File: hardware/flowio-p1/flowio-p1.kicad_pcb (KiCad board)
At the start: 4 copper layers, 90 x 75 mm, 139 parts, among them J1 DC-005, J10 VALVE, J11 VALVE, J12 VALVE, J13 VALVE, J14 VALVE, J15 VALVE, J16 VALVE, J17 VALVE, J18 DEBUG-UART, J19 DEBUG-GPIO, J2 USB-C, J5 XH-4P, J6 XH-4P, J7 XH-4P, J8 XH-4P, J9 XH-4P, Q10 AO3400A, Q11 SS8050, Q12 SS8050, Q3 AO3400A, Q4 AO3400A, Q5 AO3400A, Q6 AO3400A, Q7 AO3400A, Q8 AO3400A, Q9 AO3400A, SW1 RST, SW2 BOOT, SW3 USER, U1 ESP32-S3-WROOM-1-N16R8, U2 TCA9548APWR, U3 TPS54331DR, U4 CH340K, U5 USBLC6-2SC6

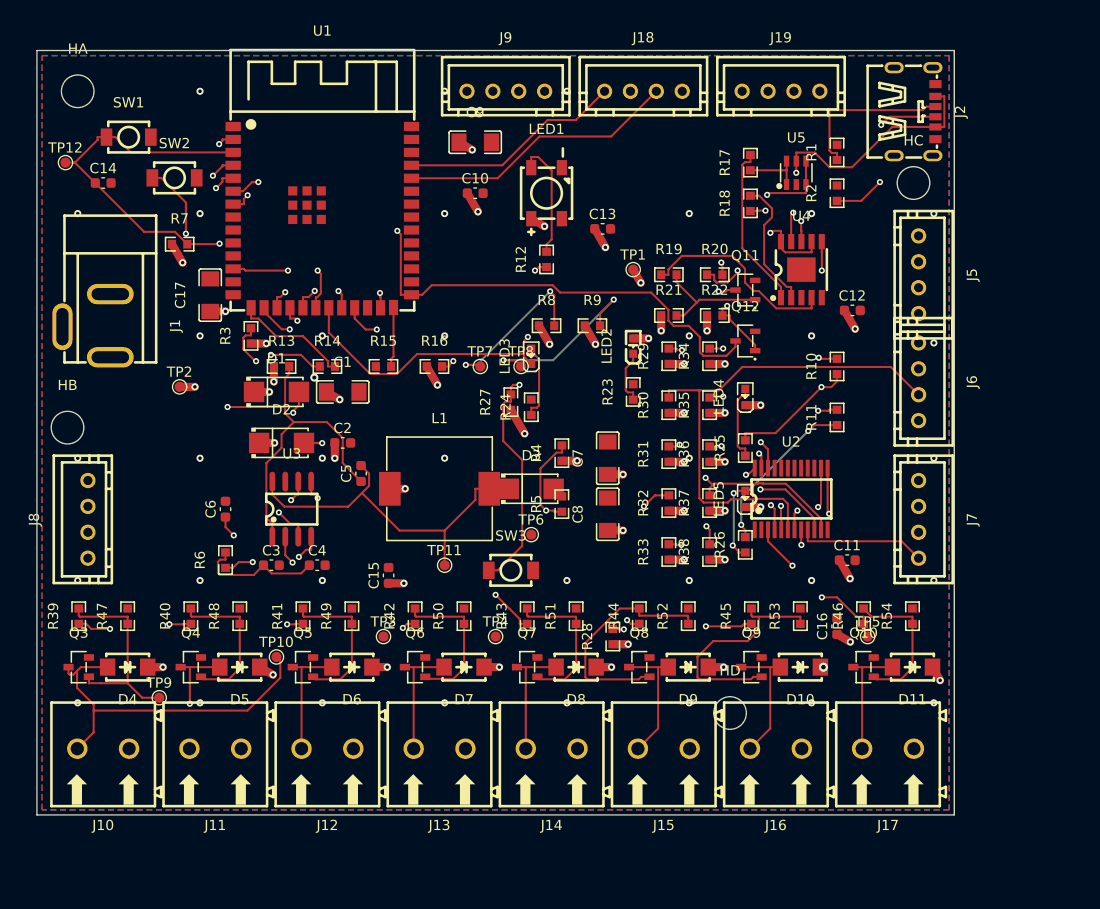
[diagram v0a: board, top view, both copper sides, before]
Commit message: feat(pcb): DRC 攻坚 17→6 未连接·其余 error 类全零 (freerouting 三轮+自研 boardgeom/netdoctor 全障碍路由)
- boardgeom: 点对旋转矩形精确距离/分层走线校验/过孔孔距规则/禁布区+板边建模
- netdoctor: 填充岛探测(PIP)/岛间跳线/焊盘逃逸/In1-In2-B.Cu 多层 BFS 路由
- 修复: 天线禁布区找回·HD移位·D10/C16/C15/C3/U3.2 电源锚·U2/U5 GND 逃逸
  (U5.2 via-in-pad)·J2.CC 走线绕行·TP8 微移·R13/R14/R29 strap 供电·GND 碎片缝合
- 遗留 6 未连接需 GUI 收尾: R13 簇/R29 簇/C3-U3.2 簇×2/GND zone 对/3V3 zone 对
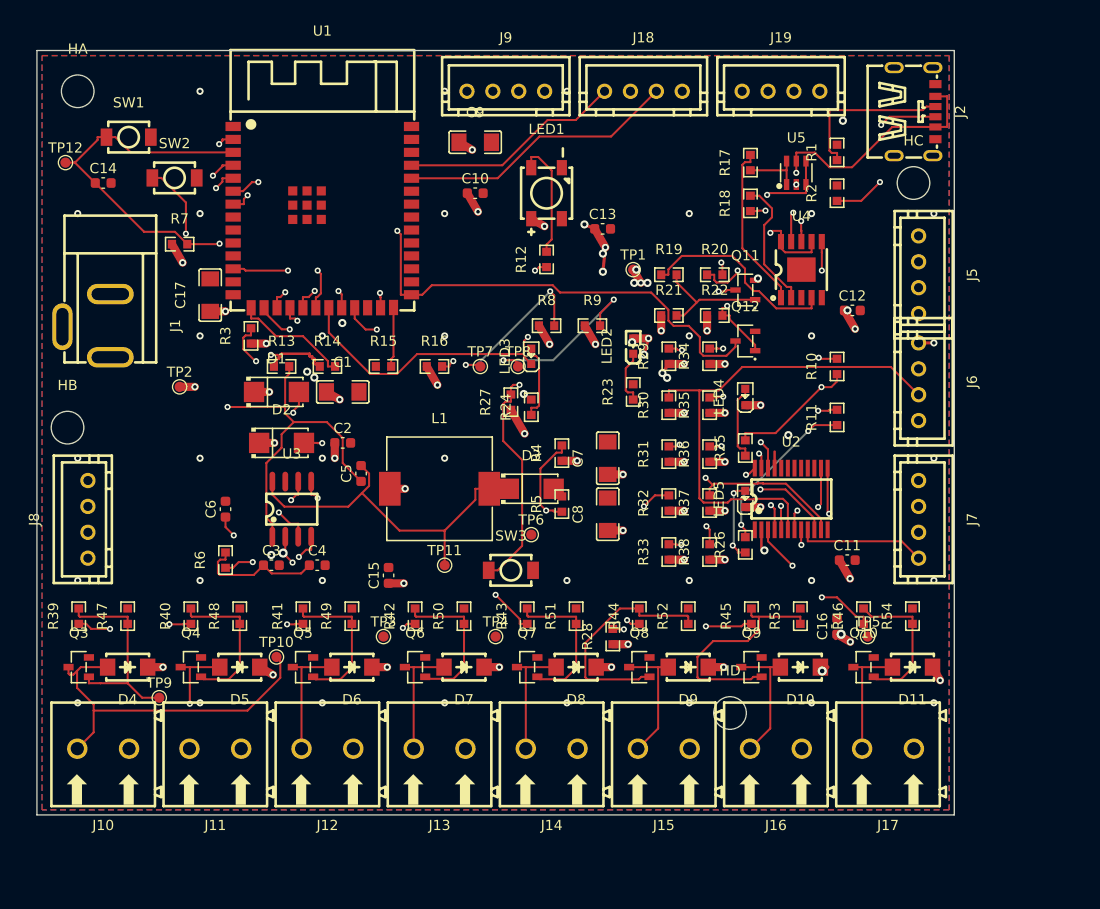
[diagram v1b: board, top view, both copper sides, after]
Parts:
- moved TP8 0.30 mm to (47.2, 31.0)
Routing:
- net +5V: track 32.8 -> 55.2 mm, vias 18 -> 20
- net +3V3: track 122.2 -> 130.5 mm, vias 39 -> 48
- net GND: track 0.00 -> 3.65 mm, vias 35 -> 44
- net USB_VBUS: track 86.6 -> 87.1 mm

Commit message: feat(pcb): T1 KRT repair_planes 全层修复 → 未连接 6→0, error 类全零!
- GND F/B/In1 + 3V3(12区11路)/5V(6区5路) In2 平面断区全接
- oracle_reconnect 连带解决 R13/R14/C3-U3.2 口袋簇 (6→0 超预期)
- 剩余仅外观类: silk_over_copper 54 + courtyard 44+13 (豁免清单)
- 环境补装 scipy/shapely + rust grid_router v0.22 + kicad_oracle v10 上游bug补丁
- 附注: min_hole_clearance 25→20 (JLC 经济档合规) + 8处 via-in-pad 需 IPC-4761 Type VII
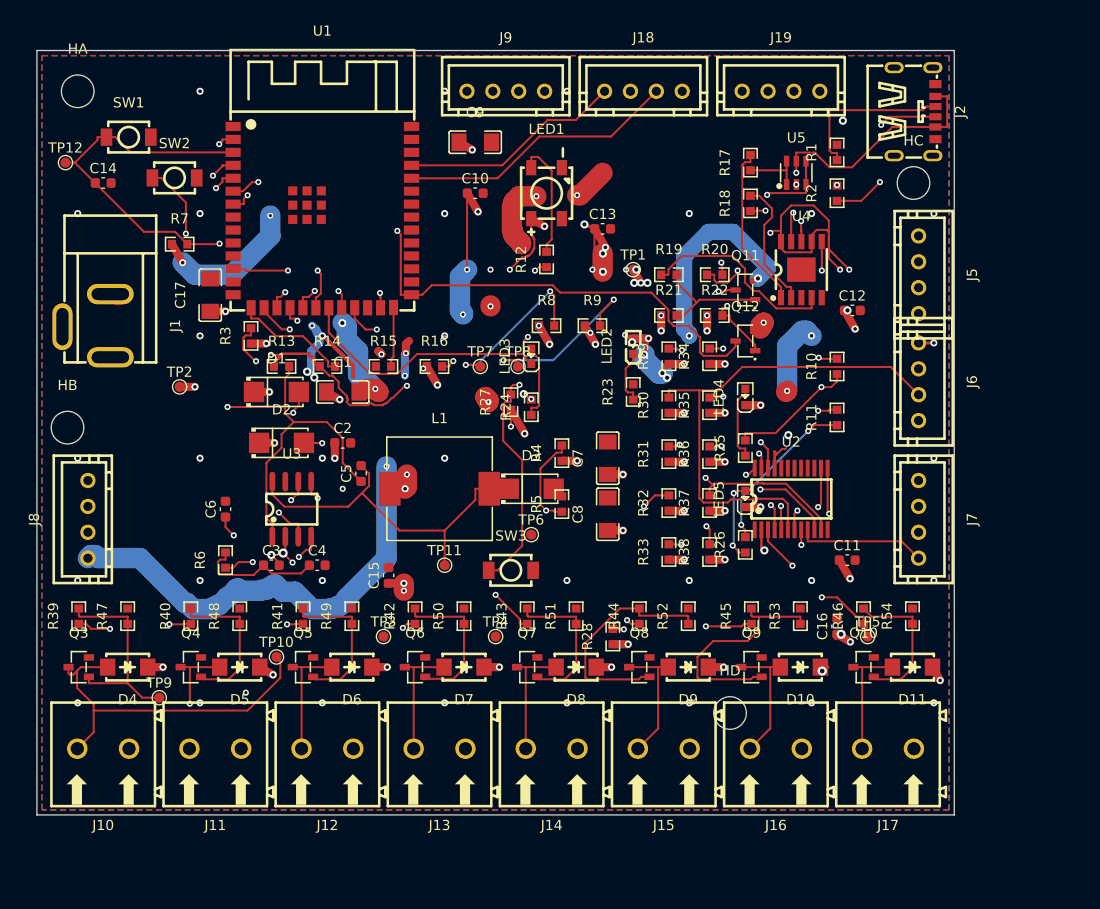
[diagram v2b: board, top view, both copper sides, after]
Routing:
- net +3V3: track 130.5 -> 285.5 mm, vias 48 -> 66
- net GND: track 3.65 -> 138.8 mm, vias 44 -> 60
- net +5V: track 55.2 -> 84.6 mm, vias 20 -> 21

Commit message: feat(T3b): PCB 重布局 100x80 + 五缺陷修复 + 26 新件 — DRC error 归零
布局 (spec T3):
- 板框 90x75 -> 100x80: 底边 J10-J17 阀带 (11mm 节距) + 右边 J20-J23 主阀/泵带
  + 传感带重排 (J5 底右角/J6 左壁/J7 顶右角, 为右边缘主阀带让位)
- 新增 PLACE: J20-J23 + R55-64/Q13-16/D12-15 右侧驱动列 (与 Q3-Q10 同域) +
  U6 XGZP6897D (44,22, LOCAL 内联手建封装: 排距7.96/节距2.54/焊盘0.9x2.0) +
  C18 + U7/R63/R64 (J1 USB-C CC 防护) + TP13 (DRV_PUMP)
- 安装孔: HA(3.4,3.4)/HC(83,12)/HB(3,28)/HD(73.5,55.7) — HD 避 J15/J16+D9 双冲突

五缺陷修复 (spec §1):
1. C9 移 (63,55) 出 J9 XH 壳体投影 (原 43,9)
2. R3 移 (21,34) 出 U1 WROOM 禁布 (本体下缘 26.1 + 3mm)
3. HD 移位 + case_geom.ST 同步 (见 T3c) — 钻孔对拍由 L2 测试守门
4. route_pcb.py: npth_min 2.0->3.5 (过孔-铜柱环外缘净空, 板界 100x80,
   缝合栅格扩展) — T4 布线不再复发; MANUAL 干线表标废弃待 T4 重推导
5. 端子高度 offset: WJ500V->XH-2P 换型自然消解 (h 14.07->6.2)

连带清除 P1.0 遗留 courtyard 冲突 (44 项): Q-D 列距 ±2.4->±3.0/+2.5,
上拉梯/LED 列/下载三极管/buck 输出链重排, SW1/SW2/R1/R2/R10/R11 微调
设计规则: 板边铜净空 0.5->0.3 (显式, JLC ≥0.3)
产物: flowio-p1.kicad_pcb (164 封装) + drc.rpt (0 error) + fab/ 全套重出
(pos 147 refs / drl M3=T5@新孔位 / gerber / BOM 39 行 146 refs / pos-jlc)
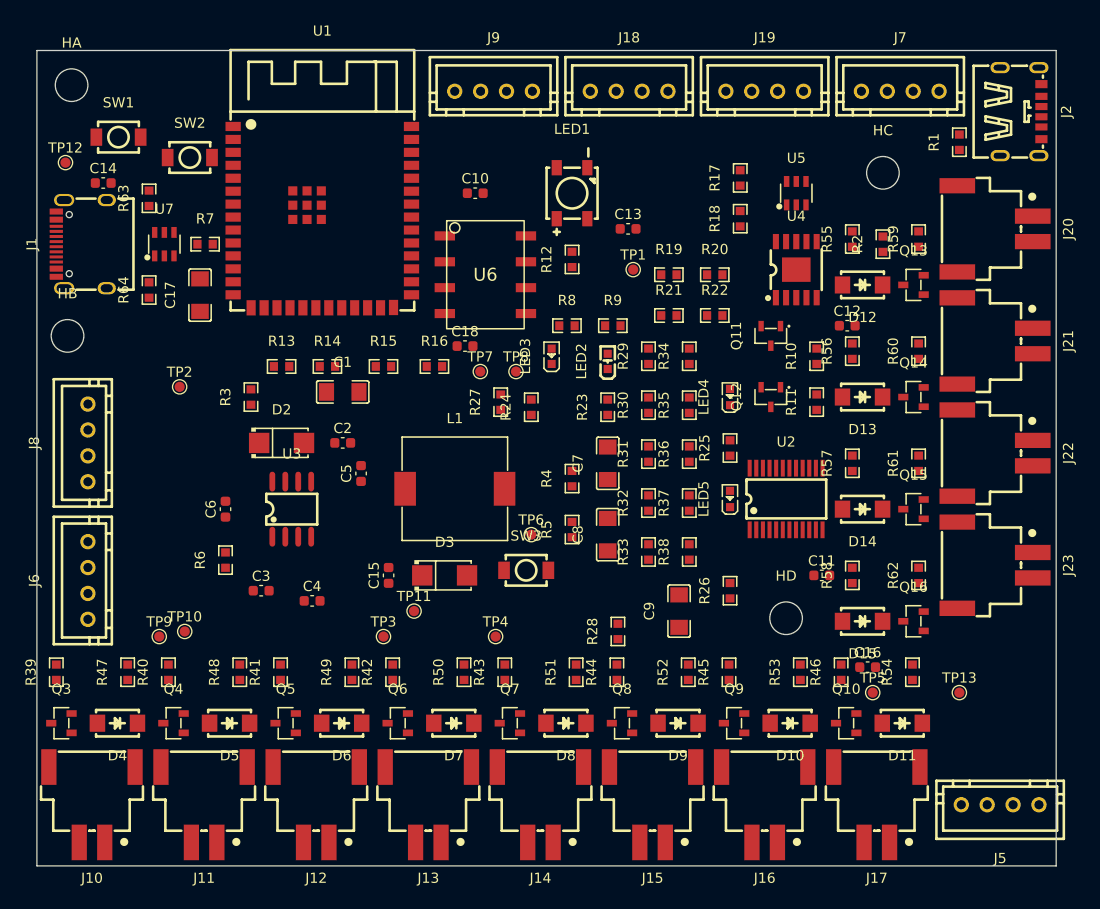
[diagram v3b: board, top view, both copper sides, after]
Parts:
- removed D1: SS34, SMA_L4.3-W2.6-LS5.2-RD
- added C18: 100nF, C_0603_1608Metric, F.Cu at (42.0, 29.0)
- added D12: SS14, SMA_L4.2-W2.6-LS5.0-RD_1, F.Cu at (81.0, 23.0)
- added D13: SS14, SMA_L4.2-W2.6-LS5.0-RD_1, F.Cu at (81.0, 34.0)
- added D14: SS14, SMA_L4.2-W2.6-LS5.0-RD_1, F.Cu at (81.0, 45.0)
- added D15: SS14, SMA_L4.2-W2.6-LS5.0-RD_1, F.Cu at (81.0, 56.0)
- added J20: VALVE, CONN-SMD_2P-P2.54_MEGASTAR_ZX-XH2.54-2PWT, F.Cu at (94.0, 17.5)
- added J21: VALVE, CONN-SMD_2P-P2.54_MEGASTAR_ZX-XH2.54-2PWT, F.Cu at (94.0, 28.5)
- added J22: VALVE, CONN-SMD_2P-P2.54_MEGASTAR_ZX-XH2.54-2PWT, F.Cu at (94.0, 39.5)
- added J23: PUMP, CONN-SMD_2P-P2.54_MEGASTAR_ZX-XH2.54-2PWT, F.Cu at (94.0, 50.5)
- added Q13: AO3400A, SOT-23-3_L2.9-W1.3-P1.90-LS2.4-BR, F.Cu at (86.0, 23.0)
- added Q14: AO3400A, SOT-23-3_L2.9-W1.3-P1.90-LS2.4-BR, F.Cu at (86.0, 34.0)
- added Q15: AO3400A, SOT-23-3_L2.9-W1.3-P1.90-LS2.4-BR, F.Cu at (86.0, 45.0)
- added Q16: AO3400A, SOT-23-3_L2.9-W1.3-P1.90-LS2.4-BR, F.Cu at (86.0, 56.0)
- added R55: 1k, R0603, F.Cu at (80.0, 18.5)
- added R56: 1k, R0603, F.Cu at (80.0, 29.5)
- added R57: 1k, R0603, F.Cu at (80.0, 40.5)
- added R58: 1k, R0603, F.Cu at (80.0, 51.5)
- added R59: 10k, R0603, F.Cu at (86.5, 18.5)
- added R60: 10k, R0603, F.Cu at (86.5, 29.5)
- added R61: 10k, R0603, F.Cu at (86.5, 40.5)
- added R62: 10k, R0603, F.Cu at (86.5, 51.5)
- added R63: 5.1k, R0603, F.Cu at (11.0, 14.5)
- added R64: 5.1k, R0603, F.Cu at (11.0, 23.5)
- added TP13: DRV_PUMP, TestPoint_Pad_D1.0mm, F.Cu at (90.5, 63.0)
- added U6: XGZP6897D, LOCAL:XGZP6897D-SOP8-W7.96-P2.54, F.Cu at (44.0, 22.0)
- added U7: USBLC6-2SC6, SOT-23-6_L2.9-W1.6-P0.95-LS2.8-BL, F.Cu at (12.5, 19.0)
- J1: value DC-005 -> USB-C PWR; footprint DC-IN-TH_DC005 -> USB-C_SMD-TYPE-C-31-M-12_1
- J10, J11, J12, J13, J14, J15, J16, J17: footprint CONN-TH_2P-P5.00_WJ500V-5.08-2P -> CONN-SMD_2P-P2.54_MEGASTAR_ZX-XH2.54-2PWT
- moved J6 83.8 mm to (5.00, 52.0), turned to 90 degrees
- moved J5 52.6 mm to (94.5, 74.0), turned to 180 degrees
- moved C9 50.2 mm to (63.0, 55.0), turned to 90 degrees
- moved J7 42.0 mm to (84.7, 4.00), turned to 0 degrees
- moved R1 12.0 mm to (90.5, 9.00)
- moved D3 12.0 mm to (40.0, 51.5)
- moved HD 10.8 mm to (73.5, 55.7)
- moved J2 10.4 mm to (96.4, 6.00)
- moved TP10 9.34 mm to (14.5, 57.0)
- moved HB 9.00 mm to (3.00, 28.0)
- moved J1 8.06 mm to (4.50, 19.0), turned to 90 degrees
- moved J8 7.50 mm to (5.00, 38.5)
- moved R2 6.73 mm to (83.0, 19.0)
- moved Q12 6.04 mm to (72.0, 34.0), turned to 90 degrees
- moved R3 6.00 mm to (21.0, 34.0)
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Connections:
- J1 pad 1: DC_IN -> GND
- J1 pad 3: (no net) -> GND
- U1 pad 10: (no net) -> IO17
- U1 pad 11: (no net) -> IO18
- U1 pad 8: (no net) -> IO15
- U1 pad 9: (no net) -> IO16
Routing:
- net +3V3: track 285.5 -> 0.00 mm, vias 66 -> 0
- net BTN_USER: track 151.0 -> 0.00 mm, vias 2 -> 0
- net GND: track 138.8 -> 0.00 mm, vias 60 -> 0
- net BOOT: track 126.5 -> 0.00 mm, vias 3 -> 0
- net EN: track 89.0 -> 0.00 mm, vias 2 -> 0
- net USB_VBUS: track 87.1 -> 0.00 mm, vias 2 -> 0
- net +5V: track 84.6 -> 0.00 mm, vias 21 -> 0
- net S4_SDA: track 78.4 -> 0.00 mm, vias 2 -> 0
- net I2C_SDA: track 77.6 -> 0.00 mm, vias 4 -> 0
- net S4_SCL: track 76.1 -> 0.00 mm, vias 1 -> 0
- net S5_SDA: track 72.8 -> 0.00 mm, vias 2 -> 0
- net LED_USER: track 69.7 -> 0.00 mm, vias 1 -> 0
- net S5_SCL: track 68.8 -> 0.00 mm, vias 2 -> 0
- net I2C_SCL: track 68.4 -> 0.00 mm, vias 4 -> 0
- net IO21: track 67.0 -> 0.00 mm, vias 2 -> 0
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- removed copper zone on In2.Cu, net +3V3
- removed copper zone on In2.Cu, net +5V
- removed copper zone on B.Cu, net GND
- removed copper zone on F.Cu, net GND
- removed copper zone on In1.Cu, net GND
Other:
- board size 90 x 75 mm -> 100 x 80 mm

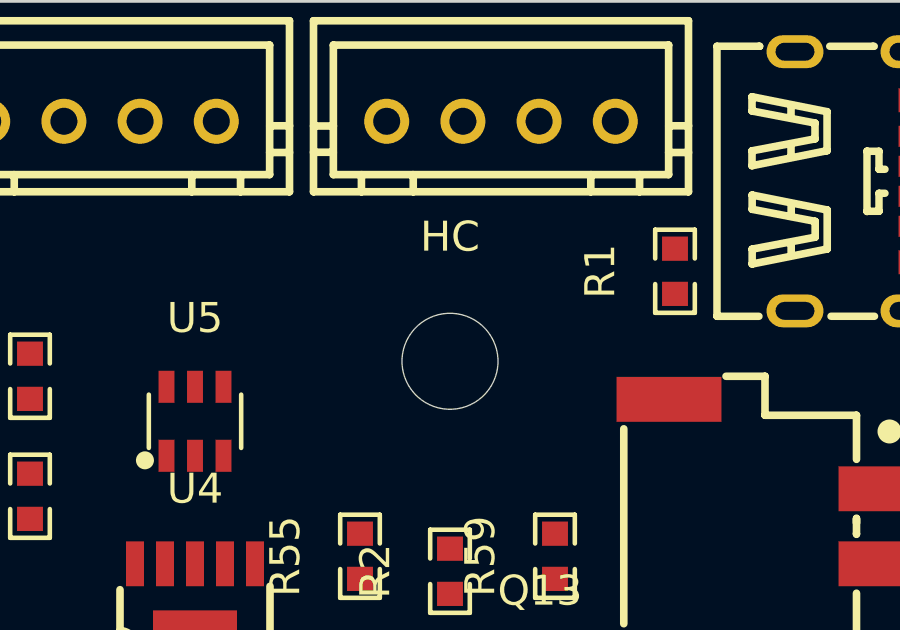
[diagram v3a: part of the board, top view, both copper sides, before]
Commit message: feat(T3c): 装配链同步 100x80 — 壳体/孪生/器件几何层全绿 (L1-L3 29/0, L5 28/0)
- case_geom: BW/BH=100/80 (OW/OH 105.8x85.8), ST=新四孔 (HC 83,12.5 避 J7 OBB
  0.3mm 裕量), CUTS 13 侧槽 (L:J1 USB-C/J8/J6 + R:J2/J20-J23 + T:J9/J18/J19/J7
  + B:J5@94.5), TERM_X 11mm 节距带, TERM_RELIEF 重定 y 带, TALLEST 14.07→9.5
  (WJ500V 退役, XGZP 倒钩管为最高件) — 壳总高 26.07→21.5
- ingest: CURATED 换血 (-DC005/-WJ500V +C165948 USB-C +C7429671 XH-2P) +
  U6 淘宝件特例段 (CURATED_NOPART, lcsc="") + pneumatic_devices 段保留守卫
  (防重跑覆写丢 T1 数据); devices.json 34 条/refs 147
- make_flows: POS_P11 过渡表删除 (真实 pos 全覆盖) + air 曲线按 rot 推导
  出线方向 (J20-J23 右壁 +X, J10-J17 底壁 +Y)
- 测试: T1 21 连接器/34 C 号(推导注明)/BOM 146 位号; KNOWN_ISSUES/HOLE_CLASH/
  VIA_BOSS 白名单清零 (五缺陷修复回归即红); T3 抽样 12 落位壁 + drop T@71.4;
  L2 钻孔按 Ø3.2 直径检索工具 (M3 工具号 T9→T5, 对拍语义不变)
- scene.js 回退 bbox 同源 105.8x85.8x21.5; 壳/网格/flows/hotspots 全部重出
- device_graph: 21↔21 完美匹配 True, flows 交叉校验 0 违例
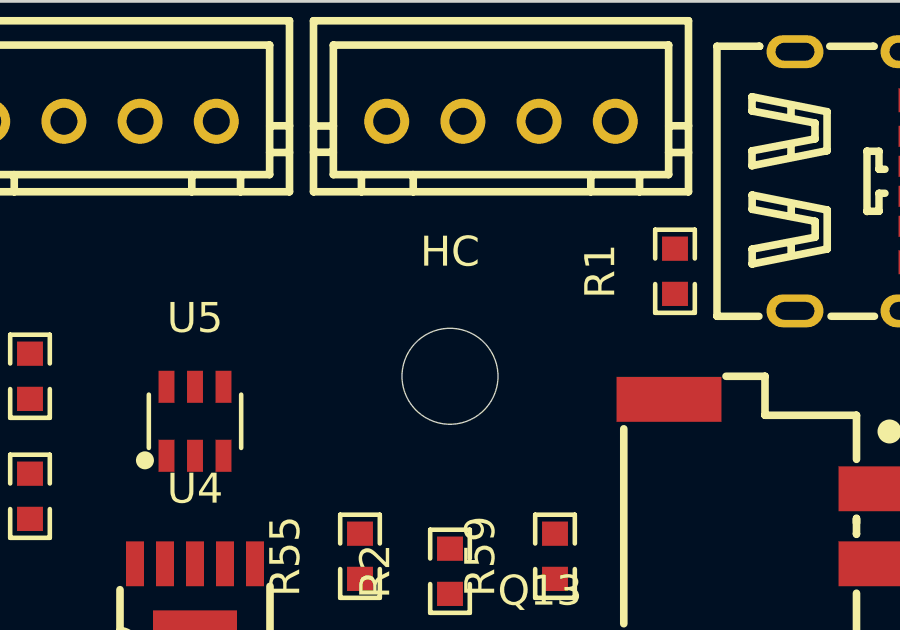
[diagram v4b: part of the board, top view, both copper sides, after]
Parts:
- moved HC 0.50 mm to (83.0, 12.5)

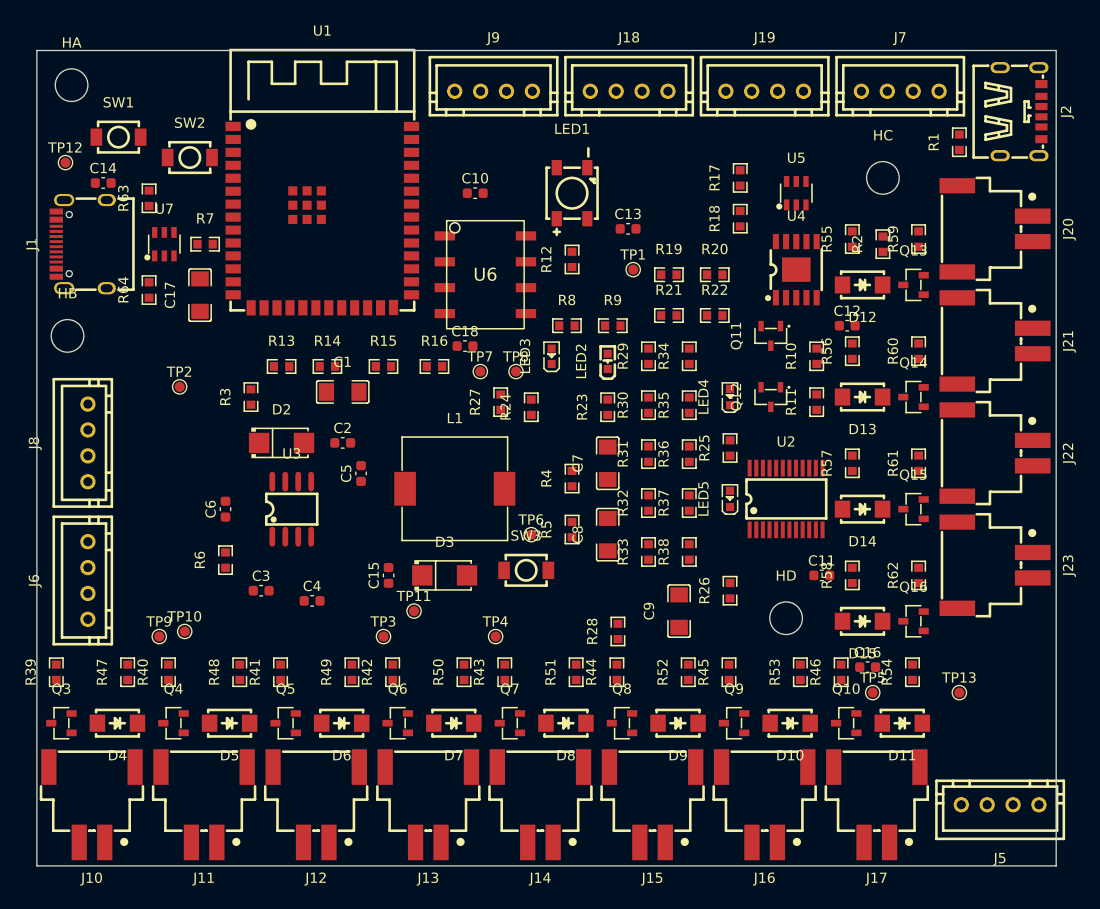
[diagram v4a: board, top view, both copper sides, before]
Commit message: feat(T4a): 布线阶段1 平面/缝合/电源过孔 — DRC 0 错 (338→183 未连)
route_pcb.py 四处硬化:
- In2 电源分区按 100x80 新布局重推导 (P1.0 L 形不覆盖右带 J20-J23):
  +5V=Z5a左上+Z5b buck带+Z5c底带+Z5d右带 (共边连通, 异优先级防
  zones_intersect) / +3V3=Z3a顶+Z3b R13/14颈+Z3c中心块; J5/J6/J8
  三枚 3V3 THT 归 freerouting F/B 收尾
- 天线 keepout 不再被误删 (规则区保留)
- P1.0 MANUAL 干线表(90x75 坐标)废弃 — 通用网表驱动布线覆盖 12 路
- 半径感知净空: XH pad r=1.9 时固定 1.7 阈值致过孔压焊盘, KiCad
  BOARD::Add 连通性把异网名静默传播给过孔 (实测 GND 缝合孔变
  DRV1/DRV2/+5V); 现按 qr+0.35+0.55 判距 + 存盘前网名完整性后验
- 5V 主干 3A: J1 VBUS 逃逸 1.5mm+双过孔, 插座分支 1.0mm, In2
  平面分发; 阶段1.8 六枚单辐条 GND 花焊盘改 FULL 实连
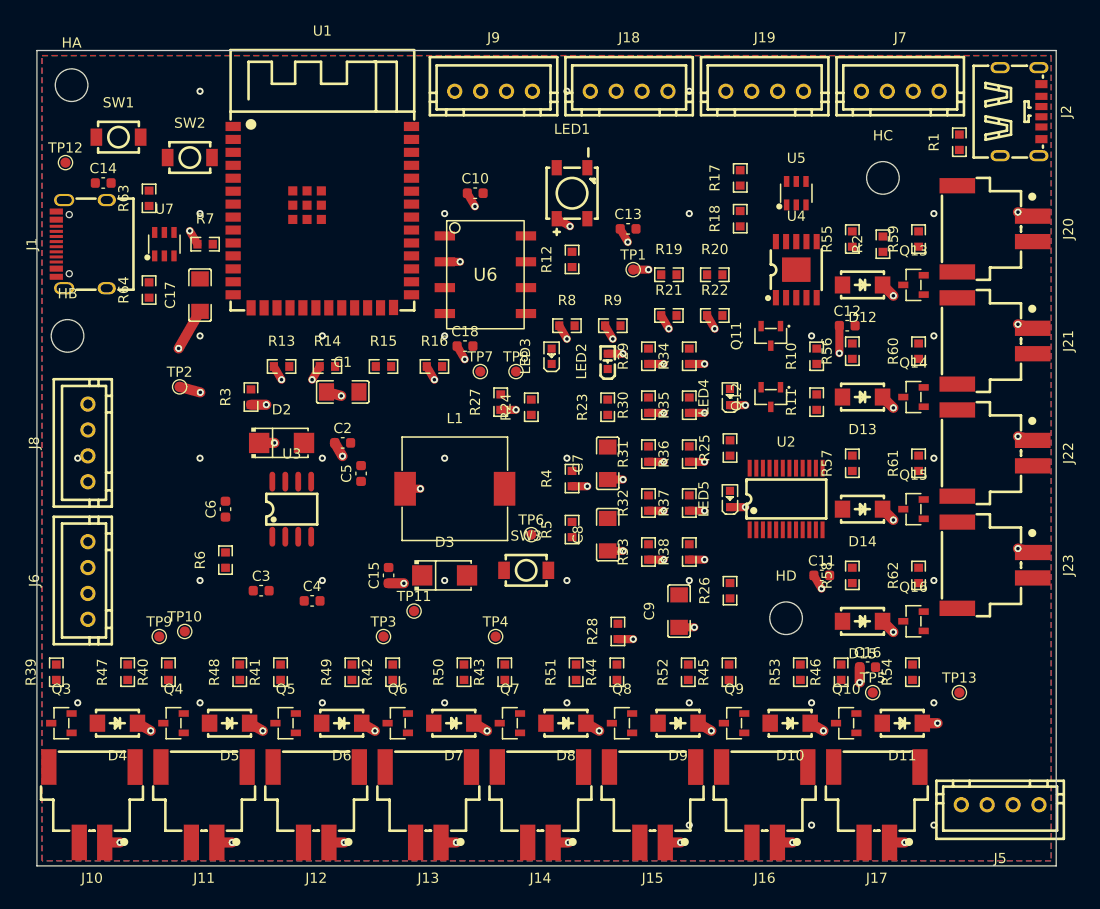
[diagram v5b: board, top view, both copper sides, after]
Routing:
- net +3V3: track 0.00 -> 55.2 mm, vias 0 -> 36
- net +5V: track 0.00 -> 51.3 mm, vias 0 -> 32
- net GND: vias 0 -> 35
- added copper zone on In2.Cu, net +3V3
- added copper zone on In2.Cu, net +5V
- added copper zone on B.Cu, net GND
- added copper zone on F.Cu, net GND
- added copper zone on In1.Cu, net GND
